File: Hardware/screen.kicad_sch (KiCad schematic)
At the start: 10 parts, among them J3 ER-CON06HT-1, J5 ER-CON50HT-1

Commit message: Schematic Done
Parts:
- J3: value ER-CON06HT-1 -> KH-FG0.5-H2.0-6PIN; LCSC (none) -> C709363; PartNumber (none) -> KH-FG0.5-H2.0-6PIN
- J5: value ER-CON50HT-1 -> HC-FPC-0.5-50P-FHH20; footprint YV:ER-CON50HT-1 -> YV:HC-FPC-0.5-50P-FHH20; LCSC (none) -> C19273943; PartNumber (none) -> HC-FPC-0.5-50P-FHH20
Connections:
- net +15V renamed +14.5V
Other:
- note added: "RGB Screen Connector"
- note added: "RS"
- note added: "Touch's I2C Connector"
- company: (none) -> Motion Composites
- title: (none) -> Strain Gauge Data Logger
- moved on the sheet: J3
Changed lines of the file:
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@@
 	(generator_version "10.0")
 	(paper "A4")
+	(title_block
+		(title "Strain Gauge Data Logger")
+		(date "2026-10-01")
+		(rev "1")
+		(company "Motion Composites")
+		(comment 1 "by Yannick Vallée, ing.")
+	)
 	(text "ER-TFT043A1-1"
 		(exclude_from_sim no)
@@
 		)
 	)
+	(text "RGB Screen Connector"
+		(exclude_from_sim no)
+		(at 182.118 20.828 0)
+		(effects
+			(font
+				(size 1.524 1.524)
+				(thickness 0.3048)
+				(bold yes)
+			)
+		)
+	)
+	(text "Touch's I2C Connector"
+		(exclude_from_sim no)
+		(at 66.294 54.356 0)
+		(effects
+			(font
+				(size 1.524 1.524)
+				(thickness 0.3048)
+				(bold yes)
+			)
+		)
+	)
+	(text "RS"
+		(exclude_from_sim no)
+		(at 208.534 120.142 0)
+		(effects
+			(font
+				(size 1.524 1.524)
+			)
+		)
+	)
 	(text "https://docs.espressif.com/projects/esp-iot-solution/en/latest/display/lcd/rgb_lcd.html"
 		(exclude_from_sim no)
@@
 	)
 	(no_connect
-		(at 99.06 125.73)
+		(at 90.17 85.09)
 	)
 	(no_connect
@@
 	(wire
 		(pts
-			(xy 91.44 110.49) (xy 91.44 105.41)
+			(xy 82.55 69.85) (xy 82.55 64.77)
 		)
 		(stroke
@@
 	(wire
 		(pts
-			(xy 72.39 118.11) (xy 93.98 118.11)
+			(xy 63.5 77.47) (xy 85.09 77.47)
 		)
 		(stroke
@@
 	(wire
 		(pts
-			(xy 93.98 113.03) (xy 91.44 113.03)
+			(xy 85.09 72.39) (xy 82.55 72.39)
 		)
 		(stroke
@@
 	(wire
 		(pts
-			(xy 72.39 107.95) (xy 93.98 107.95)
+			(xy 63.5 67.31) (xy 85.09 67.31)
 		)
 		(stroke
@@
 	(wire
 		(pts
-			(xy 72.39 120.65) (xy 93.98 120.65)
+			(xy 63.5 80.01) (xy 85.09 80.01)
 		)
 		(stroke
@@
 	(wire
 		(pts
-			(xy 93.98 110.49) (xy 91.44 110.49)
+			(xy 85.09 69.85) (xy 82.55 69.85)
 		)
 		(stroke
@@
 	(wire
 		(pts
-			(xy 91.44 113.03) (xy 91.44 123.19)
+			(xy 82.55 72.39) (xy 82.55 82.55)
 		)
 		(stroke
@@
 	(wire
 		(pts
-			(xy 72.39 115.57) (xy 93.98 115.57)
+			(xy 63.5 74.93) (xy 85.09 74.93)
 		)
 		(stroke
@@
 		)
 	)
-	(label "RS"
-		(at 207.01 120.65 0)
-		(effects
-			(font
-				(size 1.524 1.524)
-			)
-			(justify left bottom)
-		)
-	)
 	(label "DS11"
 		(at 193.04 69.85 0)
@@
 	(hierarchical_label "Touch-SDA"
 		(shape bidirectional)
-		(at 72.39 118.11 180)
+		(at 63.5 77.47 180)
 		(effects
 			(font
@@
 	(hierarchical_label "Touch-SCL"
 		(shape input)
-		(at 72.39 120.65 180)
+		(at 63.5 80.01 180)
 		(effects
 			(font
@@
 	(hierarchical_label "Touch-INT"
 		(shape output)
-		(at 72.39 115.57 180)
+		(at 63.5 74.93 180)
 		(effects
 			(font
@@
 	(hierarchical_label "Touch-RST"
 		(shape input)
-		(at 72.39 107.95 180)
+		(at 63.5 67.31 180)
 		(effects
 			(font
@@
 			)
 		)
-		(property "Value" "ER-CON50HT-1"
+		(property "Value" "HC-FPC-0.5-50P-FHH20"
 			(at 224.79 95.6055 0)
 			(show_name no)
@@
 			)
 		)
-		(property "Footprint" "YV:ER-CON50HT-1"
+		(property "Footprint" "YV:HC-FPC-0.5-50P-FHH20"
 			(at 222.25 92.71 0)
 			(hide yes)
@@
 			)
 		)
-		(property "Description" "\"Generic connectable mounting pin connector, single row, 01x50, script generated\""
+		(property "Description" "0.3mm 0.5mm 2mm 50P Copper Double-Sided Contacts, Top and Bottom Entry Flip-Top Gold Surface Mount, Right Angle SMD,P=0.5mm,Surface Mount，Right Angle FFC, FPC (Flat Flexible) , -25℃~+85℃"
+			(at 222.25 92.71 0)
+			(hide yes)
+			(show_name no)
+			(do_not_autoplace no)
+			(effects
+				(font
+					(size 1.27 1.27)
+				)
+			)
+		)
+		(property "PartNumber" "HC-FPC-0.5-50P-FHH20"
+			(at 222.25 92.71 0)
+			(hide yes)
+			(show_name no)
+			(do_not_autoplace no)
+			(effects
+				(font
+					(size 1.27 1.27)
+				)
+			)
+		)
+		(property "LCSC" "C19273943"
 			(at 222.25 92.71 0)
 			(hide yes)
@@
 	(symbol
 		(lib_id "YV-library:ER-CON06HT-1")
-		(at 99.06 113.03 0)
+		(at 90.17 72.39 0)
 		(unit 1)
 		(body_style 1)
@@
 		(fields_autoplaced yes)
 		(property "Reference" "J3"
-			(at 101.6 113.3855 0)
+			(at 92.71 72.7455 0)
 			(show_name no)
 			(do_not_autoplace no)
@@
 			)
 		)
-		(property "Value" "ER-CON06HT-1"
-			(at 101.6 115.9255 0)
+		(property "Value" "KH-FG0.5-H2.0-6PIN"
+			(at 92.71 75.2855 0)
 			(show_name no)
 			(do_not_autoplace no)
@@
 		)
 		(property "Footprint" "YV:ER-CON06HT-1"
-			(at 99.06 113.03 0)
+			(at 90.17 72.39 0)
 			(hide yes)
 			(show_name no)
@@
 		)
 		(property "Datasheet" "https://www.buydisplay.com/download/connector/ER-CON06HT-1.pdf"
-			(at 99.06 113.03 0)
+			(at 90.17 72.39 0)
 			(hide yes)
 			(show_name no)
@@
 		)
 		(property "Description" "6 Pins 0.5mm Pitch ZIF Connector"
-			(at 99.06 113.03 0)
+			(at 90.17 72.39 0)
+			(hide yes)
+			(show_name no)
+			(do_not_autoplace no)
+			(effects
+				(font
+					(size 1.27 1.27)
+				)
+			)
+		)
+		(property "PartNumber" "KH-FG0.5-H2.0-6PIN"
+			(at 90.17 72.39 0)
+			(hide yes)
+			(show_name no)
+			(do_not_autoplace no)
+			(effects
+				(font
+					(size 1.27 1.27)
+				)
+			)
+		)
+		(property "LCSC" "C709363"
+			(at 90.17 72.39 0)
 			(hide yes)
 			(show_name no)
@@
 	(symbol
 		(lib_id "power:GND")
-		(at 91.44 123.19 0)
+		(at 82.55 82.55 0)
 		(unit 1)
 		(body_style 1)
@@
 		(fields_autoplaced yes)
 		(property "Reference" "#PWR074"
-			(at 91.44 129.54 0)
+			(at 82.55 88.9 0)
 			(hide yes)
 			(show_name no)
@@
 		)
 		(property "Value" "GND"
-			(at 91.44 128.27 0)
+			(at 82.55 87.63 0)
 			(hide yes)
 			(show_name no)
@@
 		)
 		(property "Footprint" ""
-			(at 91.44 123.19 0)
+			(at 82.55 82.55 0)
 			(hide yes)
 			(show_name no)
@@
 		)
 		(property "Datasheet" ""
-			(at 91.44 123.19 0)
+			(at 82.55 82.55 0)
 			(hide yes)
 			(show_name no)
@@
 		)
 		(property "Description" "Power symbol creates a global label with name \"GND\" , ground"
-			(at 91.44 123.19 0)
+			(at 82.55 82.55 0)
 			(hide yes)
 			(show_name no)
@@
 		(in_pos_files yes)
 		(dnp no)
-		(fields_autoplaced yes)
 		(property "Reference" "#PWR076"
 			(at 181.61 140.97 0)
@@
 			)
 		)
-		(property "Value" "+15V"
-			(at 181.61 132.08 0)
+		(property "Value" "+14.5V"
+			(at 178.054 133.096 0)
 			(show_name no)
 			(do_not_autoplace no)
@@
 					(size 1.27 1.27)
 				)
+				(justify left)
 			)
 		)
@@
 	(symbol
 		(lib_id "power:+3.3V")
-		(at 91.44 105.41 0)
+		(at 82.55 64.77 0)
 		(unit 1)
 		(body_style 1)
@@
 		(fields_autoplaced yes)
 		(property "Reference" "#PWR075"
-			(at 91.44 109.22 0)
+			(at 82.55 68.58 0)
 			(hide yes)
 			(show_name no)
@@
 		)
 		(property "Value" "+3.3V"
-			(at 91.44 100.33 0)
+			(at 82.55 59.69 0)
 			(show_name no)
 			(do_not_autoplace no)
@@
 		)
 		(property "Footprint" ""
-			(at 91.44 105.41 0)
+			(at 82.55 64.77 0)
 			(hide yes)
 			(show_name no)
@@
 		)
 		(property "Datasheet" ""
-			(at 91.44 105.41 0)
+			(at 82.55 64.77 0)
 			(hide yes)
 			(show_name no)
@@
 		)
 		(property "Description" "Power symbol creates a global label with name \"+3.3V\""
-			(at 91.44 105.41 0)
+			(at 82.55 64.77 0)
 			(hide yes)
 			(show_name no)

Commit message: Layout cleaned
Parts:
- renumbered J5 to J10, J3 to J9, R26 to R20, R23 to R21, R21 to R23, R30 to R25, R29 to R26, R28 to R27, R27 to R28
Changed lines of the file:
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@@
 		(dnp no)
 		(fields_autoplaced yes)
-		(property "Reference" "J5"
+		(property "Reference" "J10"
 			(at 224.79 93.0655 0)
 			(show_name no)
@@
 			(project "esp32-V2"
 				(path "/cee18f8d-8618-44b5-96f4-3f3967d85a92/2237552a-455d-4ac3-8a7b-2b14a3b9afb4"
-					(reference "J5")
+					(reference "J10")
 					(unit 1)
 				)
@@
 		(in_pos_files yes)
 		(dnp yes)
-		(property "Reference" "R26"
+		(property "Reference" "R20"
 			(at 161.798 143.002 90)
 			(show_name no)
@@
 			(project "esp32-V2"
 				(path "/cee18f8d-8618-44b5-96f4-3f3967d85a92/2237552a-455d-4ac3-8a7b-2b14a3b9afb4"
-					(reference "R26")
+					(reference "R20")
 					(unit 1)
 				)
@@
 		(dnp no)
 		(fields_autoplaced yes)
-		(property "Reference" "J3"
+		(property "Reference" "J9"
 			(at 92.71 72.7455 0)
 			(show_name no)
@@
 			(project "esp32-V2"
 				(path "/cee18f8d-8618-44b5-96f4-3f3967d85a92/2237552a-455d-4ac3-8a7b-2b14a3b9afb4"
-					(reference "J3")
+					(reference "J9")
 					(unit 1)
 				)
@@
 		(in_pos_files yes)
 		(dnp no)
-		(property "Reference" "R28"
+		(property "Reference" "R27"
 			(at 148.844 162.306 90)
 			(show_name no)
@@
 			(project "esp32-V2"
 				(path "/cee18f8d-8618-44b5-96f4-3f3967d85a92/2237552a-455d-4ac3-8a7b-2b14a3b9afb4"
-					(reference "R28")
+					(reference "R27")
 					(unit 1)
 				)
@@
 		(in_pos_files yes)
 		(dnp no)
-		(property "Reference" "R30"
+		(property "Reference" "R25"
 			(at 161.544 162.306 90)
 			(show_name no)
@@
 			(project "esp32-V2"
 				(path "/cee18f8d-8618-44b5-96f4-3f3967d85a92/2237552a-455d-4ac3-8a7b-2b14a3b9afb4"
-					(reference "R30")
+					(reference "R25")
 					(unit 1)
 				)
@@
 		(in_pos_files yes)
 		(dnp no)
-		(property "Reference" "R23"
+		(property "Reference" "R21"
 			(at 155.448 143.002 90)
 			(show_name no)
@@
 			(project "esp32-V2"
 				(path "/cee18f8d-8618-44b5-96f4-3f3967d85a92/2237552a-455d-4ac3-8a7b-2b14a3b9afb4"
-					(reference "R23")
+					(reference "R21")
 					(unit 1)
 				)
@@
 		(in_pos_files yes)
 		(dnp yes)
-		(property "Reference" "R29"
+		(property "Reference" "R26"
 			(at 155.194 162.306 90)
 			(show_name no)
@@
 			(project "esp32-V2"
 				(path "/cee18f8d-8618-44b5-96f4-3f3967d85a92/2237552a-455d-4ac3-8a7b-2b14a3b9afb4"
-					(reference "R29")
+					(reference "R26")
 					(unit 1)
 				)
@@
 		(in_pos_files yes)
 		(dnp no)
-		(property "Reference" "R27"
+		(property "Reference" "R28"
 			(at 142.494 162.306 90)
 			(show_name no)
@@
 			(project "esp32-V2"
 				(path "/cee18f8d-8618-44b5-96f4-3f3967d85a92/2237552a-455d-4ac3-8a7b-2b14a3b9afb4"
-					(reference "R27")
+					(reference "R28")
 					(unit 1)
 				)
@@
 		(in_pos_files yes)
 		(dnp yes)
-		(property "Reference" "R21"
+		(property "Reference" "R23"
 			(at 142.494 143.256 90)
 			(show_name no)
@@
 			(project "esp32-V2"
 				(path "/cee18f8d-8618-44b5-96f4-3f3967d85a92/2237552a-455d-4ac3-8a7b-2b14a3b9afb4"
-					(reference "R21")
-					(unit 1)
-				)
+					(reference "R23")
+					(unit 1)
+				)

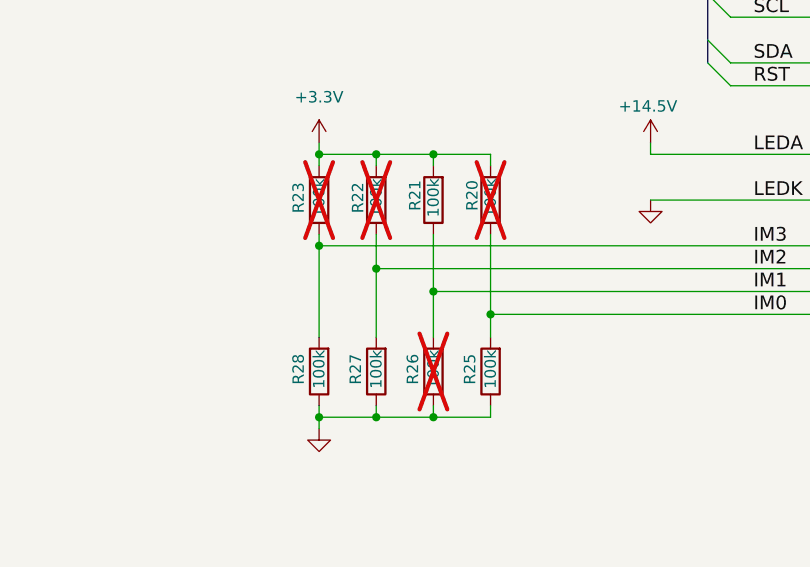
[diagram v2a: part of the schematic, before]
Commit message: Update de la librairy et du BOM
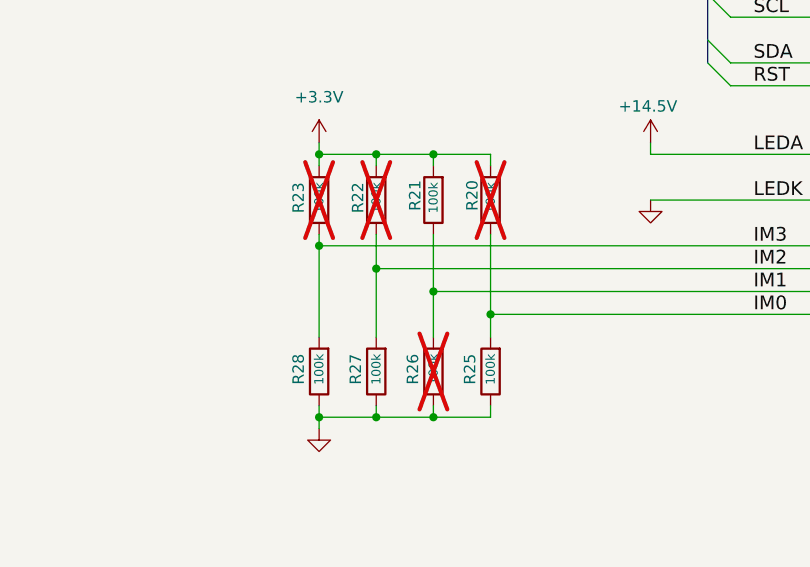
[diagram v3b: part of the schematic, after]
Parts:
- R20, R21, R22, R23, R25, R26, R27, R28: symbol Device:R -> YV-library:RES100KM-00; LCSC C2909355 -> C25741; PartNumber (none) -> 0402WGF1003TCE
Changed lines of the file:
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@@
 			)
 		)
-		(property "Description" "0.3mm 0.5mm 2mm 50P Copper Double-Sided Contacts, Top and Bottom Entry Flip-Top Gold Surface Mount, Right Angle SMD,P=0.5mm,Surface Mount，Right Angle FFC, FPC (Flat Flexible) , -25℃~+85℃"
+		(property "Description" "Connector Zif, pitch 0.5mm, height 2mm, 50 Pos, Double-Sided Contacts, Top and Bottom Entry Flip-Top Gold Surface Mount, Right Angle, Surface Mount , -25℃~+85℃"
 			(at 222.25 92.71 0)
 			(hide yes)
@@
 	)
 	(symbol
-		(lib_id "Device:R")
+		(lib_id "YV-library:RES100KM-00")
 		(at 163.83 143.51 180)
 		(unit 1)
@@
 			(effects
 				(font
-					(size 1.27 1.27)
+					(size 1.016 1.016)
 				)
 			)
@@
 			)
 		)
-		(property "Description" "Resistor"
+		(property "Description" "Res, 100kΩ, 50V, 62.5mW, Thick Film, ±1%, ±100ppm/℃, 0402,  -55℃~+155℃"
 			(at 163.83 143.51 0)
 			(hide yes)
@@
 			(effects
 				(font
-					(size 1.27 1.27)
-				)
-			)
-		)
-		(property "LCSC" "C2909355"
-			(at 163.83 143.51 90)
+					(size 1.016 1.016)
+				)
+			)
+		)
+		(property "LCSC" "C25741"
+			(at 165.608 143.51 90)
 			(hide yes)
 			(show_name no)
@@
 				(font
 					(size 1.524 1.524)
+				)
+			)
+		)
+		(property "PartNumber" "0402WGF1003TCE"
+			(at 163.83 143.51 0)
+			(hide yes)
+			(show_name no)
+			(do_not_autoplace no)
+			(effects
+				(font
+					(size 1.27 1.27)
 				)
 			)
@@
 			)
 		)
-		(property "Datasheet" "https://www.buydisplay.com/download/connector/ER-CON06HT-1.pdf"
+		(property "Datasheet" ""
 			(at 90.17 72.39 0)
 			(hide yes)
@@
 			)
 		)
-		(property "Description" "6 Pins 0.5mm Pitch ZIF Connector"
+		(property "Description" "Connector, Zif, 6 Pins, 0.5mm Pitch, Bottom Contact, -25℃~+85℃"
 			(at 90.17 72.39 0)
 			(hide yes)
@@
 	)
 	(symbol
-		(lib_id "Device:R")
+		(lib_id "YV-library:RES100KM-00")
 		(at 151.13 162.56 180)
 		(unit 1)
@@
 			(effects
 				(font
-					(size 1.27 1.27)
+					(size 1.016 1.016)
 				)
 			)
@@
 			)
 		)
-		(property "Description" "Resistor"
+		(property "Description" "Res, 100kΩ, 50V, 62.5mW, Thick Film, ±1%, ±100ppm/℃, 0402,  -55℃~+155℃"
 			(at 151.13 162.56 0)
 			(hide yes)
@@
 			(effects
 				(font
-					(size 1.27 1.27)
-				)
-			)
-		)
-		(property "LCSC" "C2909355"
-			(at 151.13 162.56 90)
+					(size 1.016 1.016)
+				)
+			)
+		)
+		(property "LCSC" "C25741"
+			(at 152.908 162.56 90)
 			(hide yes)
 			(show_name no)
@@
 				(font
 					(size 1.524 1.524)
+				)
+			)
+		)
+		(property "PartNumber" "0402WGF1003TCE"
+			(at 151.13 162.56 0)
+			(hide yes)
+			(show_name no)
+			(do_not_autoplace no)
+			(effects
+				(font
+					(size 1.27 1.27)
 				)
 			)
@@
 	)
 	(symbol
-		(lib_id "Device:R")
+		(lib_id "YV-library:RES100KM-00")
 		(at 163.83 162.56 180)
 		(unit 1)
@@
 			(effects
 				(font
-					(size 1.27 1.27)
+					(size 1.016 1.016)
 				)
 			)
@@
 			)
 		)
-		(property "Description" "Resistor"
+		(property "Description" "Res, 100kΩ, 50V, 62.5mW, Thick Film, ±1%, ±100ppm/℃, 0402,  -55℃~+155℃"
 			(at 163.83 162.56 0)
 			(hide yes)
@@
 			(effects
 				(font
-					(size 1.27 1.27)
-				)
-			)
-		)
-		(property "LCSC" "C2909355"
-			(at 163.83 162.56 90)
+					(size 1.016 1.016)
+				)
+			)
+		)
+		(property "LCSC" "C25741"
+			(at 165.608 162.56 90)
 			(hide yes)
 			(show_name no)
@@
 				(font
 					(size 1.524 1.524)
+				)
+			)
+		)
+		(property "PartNumber" "0402WGF1003TCE"
+			(at 163.83 162.56 0)
+			(hide yes)
+			(show_name no)
+			(do_not_autoplace no)
+			(effects
+				(font
+					(size 1.27 1.27)
 				)
 			)
@@
 	)
 	(symbol
-		(lib_id "Device:R")
+		(lib_id "YV-library:RES100KM-00")
 		(at 157.48 143.51 180)
 		(unit 1)
@@
 			(effects
 				(font
-					(size 1.27 1.27)
+					(size 1.016 1.016)
 				)
 			)
@@
 			)
 		)
-		(property "Description" "Resistor"
+		(property "Description" "Res, 100kΩ, 50V, 62.5mW, Thick Film, ±1%, ±100ppm/℃, 0402,  -55℃~+155℃"
 			(at 157.48 143.51 0)
 			(hide yes)
@@
 			(effects
 				(font
-					(size 1.27 1.27)
-				)
-			)
-		)
-		(property "LCSC" "C2909355"
-			(at 157.48 143.51 90)
+					(size 1.016 1.016)
+				)
+			)
+		)
+		(property "LCSC" "C25741"
+			(at 159.258 143.51 90)
 			(hide yes)
 			(show_name no)
@@
 				(font
 					(size 1.524 1.524)
+				)
+			)
+		)
+		(property "PartNumber" "0402WGF1003TCE"
+			(at 157.48 143.51 0)
+			(hide yes)
+			(show_name no)
+			(do_not_autoplace no)
+			(effects
+				(font
+					(size 1.27 1.27)
 				)
 			)
@@
 	)
 	(symbol
-		(lib_id "Device:R")
+		(lib_id "YV-library:RES100KM-00")
 		(at 157.48 162.56 180)
 		(unit 1)
@@
 			(effects
 				(font
-					(size 1.27 1.27)
+					(size 1.016 1.016)
 				)
 			)
@@
 			)
 		)
-		(property "Description" "Resistor"
+		(property "Description" "Res, 100kΩ, 50V, 62.5mW, Thick Film, ±1%, ±100ppm/℃, 0402,  -55℃~+155℃"
 			(at 157.48 162.56 0)
 			(hide yes)
@@
 			(effects
 				(font
-					(size 1.27 1.27)
-				)
-			)
-		)
-		(property "LCSC" "C2909355"
-			(at 157.48 162.56 90)
+					(size 1.016 1.016)
+				)
+			)
+		)
+		(property "LCSC" "C25741"
+			(at 159.258 162.56 90)
 			(hide yes)
 			(show_name no)
@@
 				(font
 					(size 1.524 1.524)
+				)
+			)
+		)
+		(property "PartNumber" "0402WGF1003TCE"
+			(at 157.48 162.56 0)
+			(hide yes)
+			(show_name no)
+			(do_not_autoplace no)
+			(effects
+				(font
+					(size 1.27 1.27)
 				)
 			)
@@
 	)
 	(symbol
-		(lib_id "Device:R")
+		(lib_id "YV-library:RES100KM-00")
 		(at 151.13 143.51 180)
 		(unit 1)
@@
 			(effects
 				(font
-					(size 1.27 1.27)
+					(size 1.016 1.016)
 				)
 			)
@@
 			)
 		)
-		(property "Description" "Resistor"
+		(property "Description" "Res, 100kΩ, 50V, 62.5mW, Thick Film, ±1%, ±100ppm/℃, 0402,  -55℃~+155℃"
 			(at 151.13 143.51 0)
 			(hide yes)
@@
 			(effects
 				(font
-					(size 1.27 1.27)
-				)
-			)
-		)
-		(property "LCSC" "C2909355"
-			(at 151.13 143.51 90)
+					(size 1.016 1.016)
+				)
+			)
+		)
+		(property "LCSC" "C25741"
+			(at 152.908 143.51 90)
 			(hide yes)
 			(show_name no)
@@
 				(font
 					(size 1.524 1.524)
+				)
+			)
+		)
+		(property "PartNumber" "0402WGF1003TCE"
+			(at 151.13 143.51 0)
+			(hide yes)
+			(show_name no)
+			(do_not_autoplace no)
+			(effects
+				(font
+					(size 1.27 1.27)
 				)
 			)
@@
 	)
 	(symbol
-		(lib_id "Device:R")
+		(lib_id "YV-library:RES100KM-00")
 		(at 144.78 162.56 180)
 		(unit 1)
@@
 			(effects
 				(font
-					(size 1.27 1.27)
+					(size 1.016 1.016)
 				)
 			)
@@
 			)
 		)
-		(property "Description" "Resistor"
+		(property "Description" "Res, 100kΩ, 50V, 62.5mW, Thick Film, ±1%, ±100ppm/℃, 0402,  -55℃~+155℃"
 			(at 144.78 162.56 0)
 			(hide yes)
@@
 			(effects
 				(font
-					(size 1.27 1.27)
-				)
-			)
-		)
-		(property "LCSC" "C2909355"
-			(at 144.78 162.56 90)
+					(size 1.016 1.016)
+				)
+			)
+		)
+		(property "LCSC" "C25741"
+			(at 146.558 162.56 90)
 			(hide yes)
 			(show_name no)
@@
 				(font
 					(size 1.524 1.524)
+				)
+			)
+		)
+		(property "PartNumber" "0402WGF1003TCE"
+			(at 144.78 162.56 0)
+			(hide yes)
+			(show_name no)
+			(do_not_autoplace no)
+			(effects
+				(font
+					(size 1.27 1.27)
 				)
 			)
@@
 	)
 	(symbol
-		(lib_id "Device:R")
+		(lib_id "YV-library:RES100KM-00")
 		(at 144.78 143.51 180)
 		(unit 1)
@@
 			(effects
 				(font
-					(size 1.27 1.27)
+					(size 1.016 1.016)
 				)
 			)
@@
 			)
 		)
-		(property "Description" "Resistor"
+		(property "Description" "Res, 100kΩ, 50V, 62.5mW, Thick Film, ±1%, ±100ppm/℃, 0402,  -55℃~+155℃"
 			(at 144.78 143.51 0)
 			(hide yes)
@@
 			(effects
 				(font
-					(size 1.27 1.27)
-				)
-			)
-		)
-		(property "LCSC" "C2909355"
-			(at 144.78 143.51 90)
+					(size 1.016 1.016)
+				)
+			)
+		)
+		(property "LCSC" "C25741"
+			(at 146.558 143.51 90)
 			(hide yes)
 			(show_name no)
@@
 				)
 			)
+		)
+		(property "PartNumber" "0402WGF1003TCE"
+			(at 144.78 143.51 0)
+			(hide yes)
+			(show_name no)
+			(do_not_autoplace no)
+			(effects
+				(font
+					(size 1.27 1.27)
+				)
+			)
